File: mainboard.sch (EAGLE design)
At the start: 42 parts, among them IC1 DS1307, IC2 LM2596S, J1 AVR_SPI_PRG_6PTH, Q1 32.768 kHz, U1 ATMEGA328P, U2 3.3V, U3 5V, U4 MMA7660FCR1

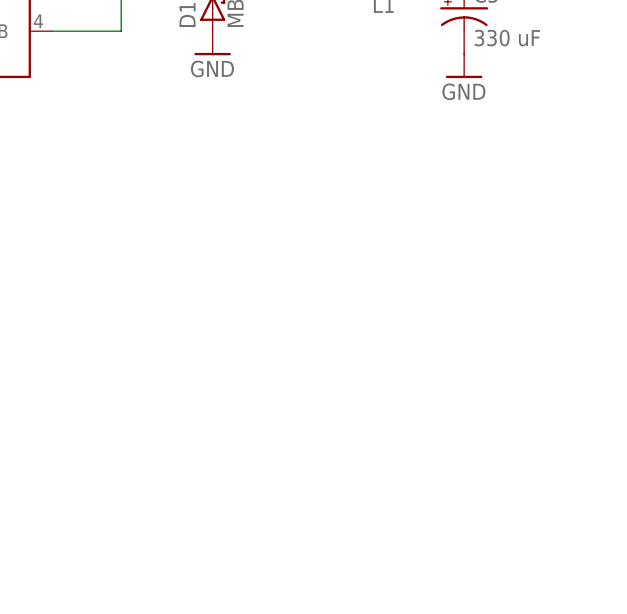
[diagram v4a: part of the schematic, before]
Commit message: Finished v1 of board design
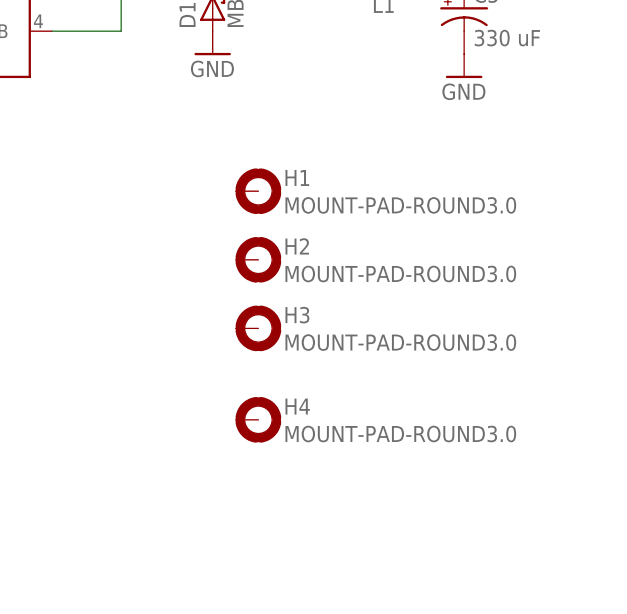
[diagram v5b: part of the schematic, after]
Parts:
- added H1, H2, H3, H4: MOUNT-PAD-ROUND3.0, holes:MOUNT-PAD-ROUND3.0
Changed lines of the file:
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@@
 <part name="GND27" library="supply1" deviceset="GND" device=""/>
 <part name="JP12" library="SparkFun-Connectors" deviceset="M06" device="SIP" value="Extra"/>
+<part name="H1" library="holes" deviceset="MOUNT-PAD-ROUND" device="3.0"/>
+<part name="H2" library="holes" deviceset="MOUNT-PAD-ROUND" device="3.0"/>
+<part name="H3" library="holes" deviceset="MOUNT-PAD-ROUND" device="3.0"/>
+<part name="H4" library="holes" deviceset="MOUNT-PAD-ROUND" device="3.0"/>
 </parts>
 <sheets>
@@
 <instance part="GND27" gate="1" x="314.96" y="-35.56" rot="R90"/>
 <instance part="JP12" gate="G$1" x="297.18" y="-30.48"/>
+<instance part="H1" gate="G$1" x="299.72" y="68.58"/>
+<instance part="H2" gate="G$1" x="299.72" y="60.96"/>
+<instance part="H3" gate="G$1" x="299.72" y="53.34"/>
+<instance part="H4" gate="G$1" x="299.72" y="43.18"/>
 </instances>
 <busses>

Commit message: Updates
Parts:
- removed H1, H2, H3, H4: MOUNT-PAD-ROUND3.0, holes:MOUNT-PAD-ROUND3.0
- removed JP12: Extra, SparkFun-Connectors:M06SIP
- added JP6: Extra, SparkFun-Connectors:M04PTH
- added JP7: MAIN_SW, SparkFun-Connectors:M02PTH
- added LED2: (no value), SparkFun-LED:LED1206
- added R16: 100, SparkFun-Resistors:RESISTOR0603
- added R17: 10k, SparkFun-Resistors:RESISTOR0603
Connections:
- removed net D4: JP12.4, U1.PD4(XCK/T0)
- removed net D7: JP12.3, U1.PD7(AIN1)
- new net 6V_ON: IC2.!ON!/OFF, U1.PD4(XCK/T0)
- new net MAIN_SW: JP7.2, R17.1, U1.PD7(AIN1)
- new net N$12: LED2.C, R16.2
- new net N$13: LED2.A, U1.PB0(ICP)
- net +5V: now also JP6.2, R17.2; no longer JP12.2
- net +6V: no longer U2.EN, U2.IN, U3.EN, U3.IN
- net A1: now also JP6.4; no longer JP12.6
- net A2: now also JP6.3; no longer JP12.5
- net BAT+: now also U2.EN, U2.IN, U3.EN, U3.IN
- net GND: now also JP6.1, JP7.1, R16.1; no longer IC2.!ON!/OFF, JP12.1
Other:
- moved on the sheet: LED1, R2

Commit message: Bring it up to date
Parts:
- R15: value 780k -> 470k
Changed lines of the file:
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@@
 <part name="C6" library="SparkFun-Capacitors" deviceset="CAP_POL" device="G" value="470uF"/>
 <part name="R14" library="SparkFun-Resistors" deviceset="RESISTOR" device="0603" value="1M"/>
-<part name="R15" library="SparkFun-Resistors" deviceset="RESISTOR" device="0603" value="780k"/>
+<part name="R15" library="SparkFun-Resistors" deviceset="RESISTOR" device="0603" value="470k"/>
 <part name="C7" library="SparkFun-Capacitors" deviceset="CAP" device="0603-CAP" value="0.1uF"/>
 <part name="GND25" library="supply1" deviceset="GND" device=""/>

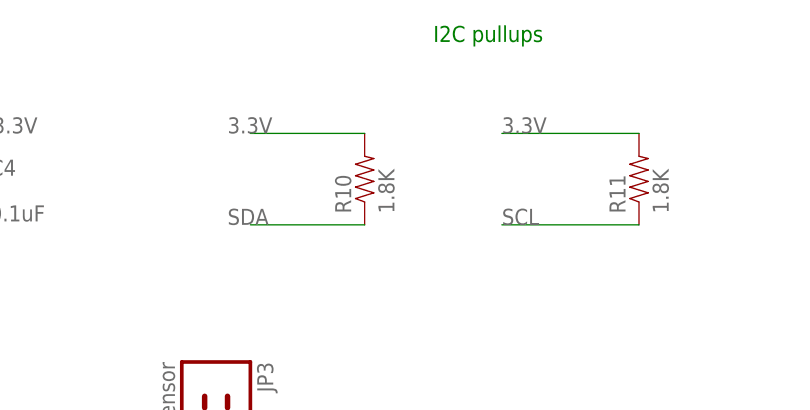
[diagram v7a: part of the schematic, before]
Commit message: Changed instances of 3.3V net to correct +3.3V net. Rerouted affected sections.
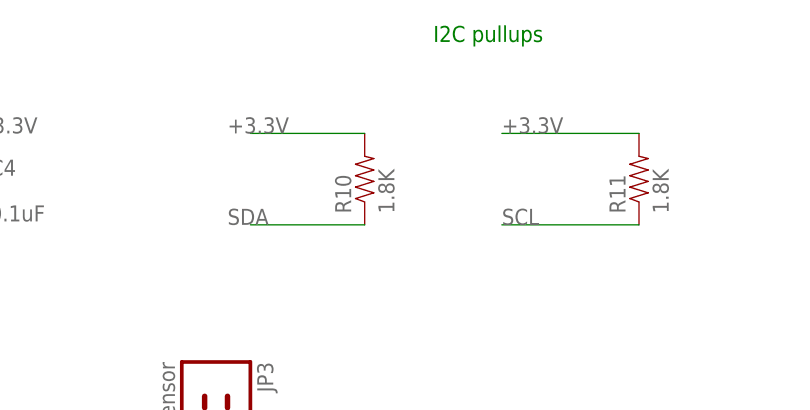
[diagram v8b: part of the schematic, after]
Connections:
- removed net 3.3V: R10.2, R11.2
- net +3.3V: now also R10.2, R11.2
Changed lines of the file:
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@@
 <junction x="121.92" y="-30.48"/>
 </segment>
-</net>
-<net name="3.3V" class="0">
 <segment>
 <pinref part="R10" gate="G$1" pin="2"/>
